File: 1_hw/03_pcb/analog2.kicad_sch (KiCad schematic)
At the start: 19 parts, among them U22 TPL0401B-10, U23 THS3491, U24 ADG1219BRJZ

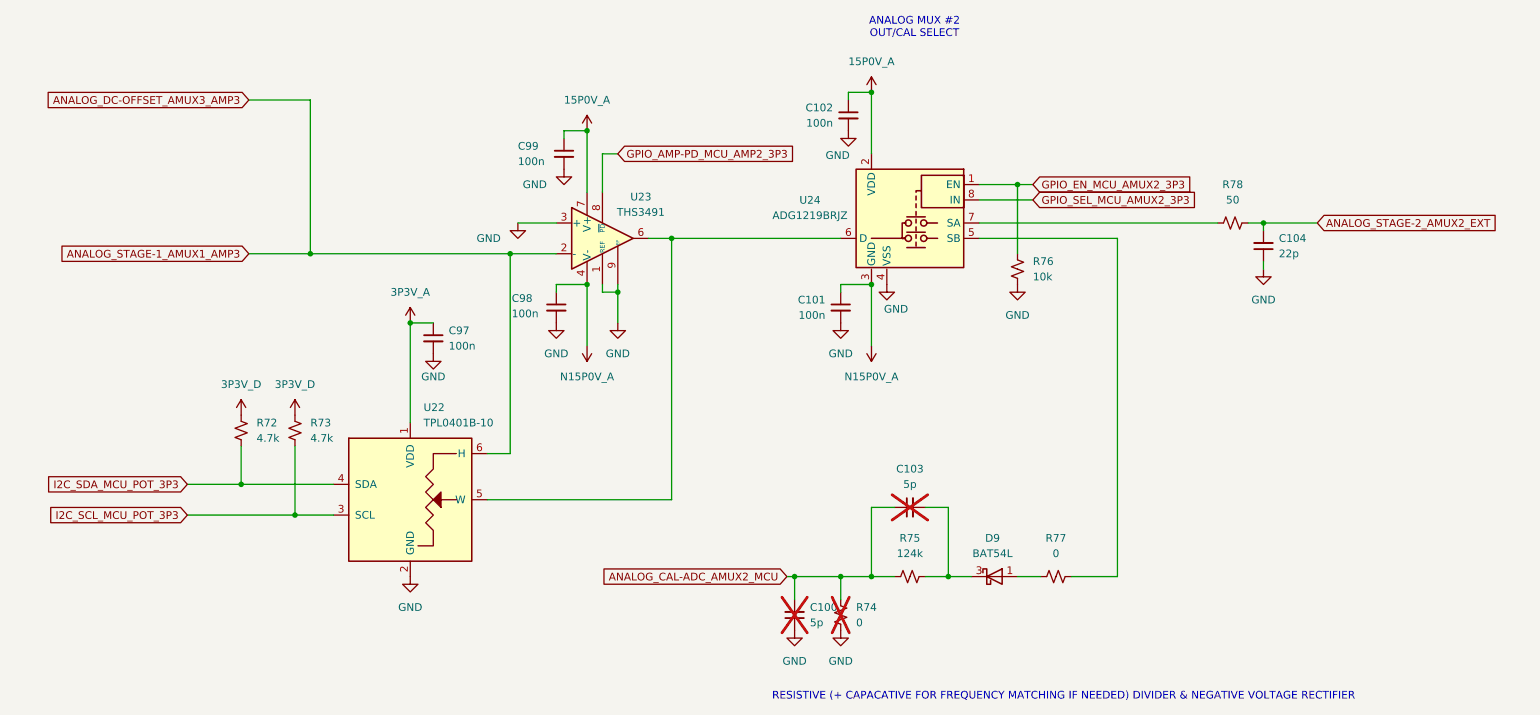
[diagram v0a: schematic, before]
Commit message: MINOR: Verified Footprints to Datasheets. Added Pull Ups on FPGA DONE/Config/SPI Chip Select Pins.
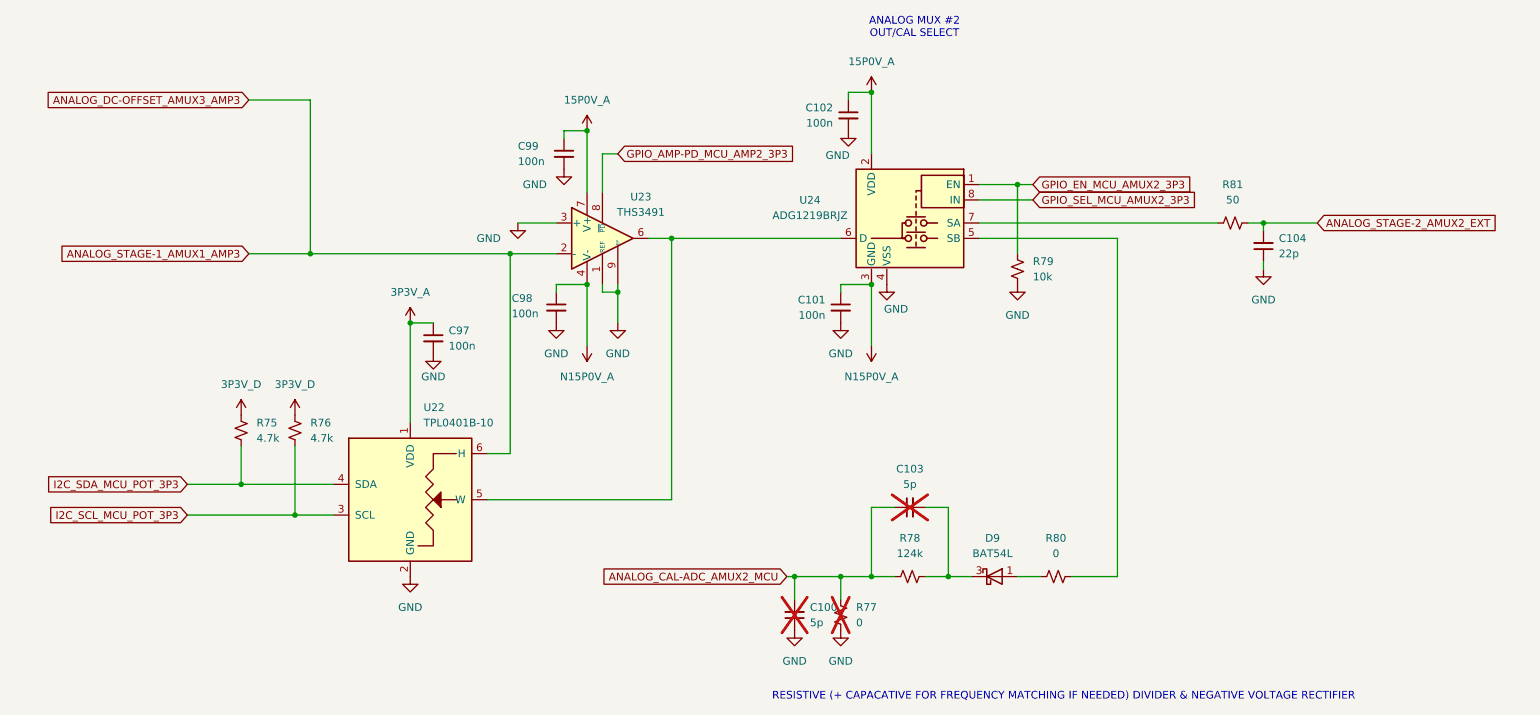
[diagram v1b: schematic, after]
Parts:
- renumbered R72 to R75, R73 to R76, R74 to R77, R75 to R78, R76 to R79, R77 to R80, R78 to R81
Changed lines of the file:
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@@
 		(dnp no)
 		(fields_autoplaced yes)
-		(property "Reference" "#PWR0257"
+		(property "Reference" "#PWR0260"
 			(at 152.4 104.14 0)
 			(effects
@@
 			(project "arb"
 				(path "/866ef9be-3b01-4288-a6e0-a2357aa17e50/e46c6640-71a3-4b78-b602-0f6be9676e36"
-					(reference "#PWR0257")
+					(reference "#PWR0260")
 					(unit 1)
 				)
@@
 		(dnp yes)
 		(fields_autoplaced yes)
-		(property "Reference" "R74"
+		(property "Reference" "R77"
 			(at 154.94 144.7799 0)
 			(effects
@@
 			(project "arb"
 				(path "/866ef9be-3b01-4288-a6e0-a2357aa17e50/e46c6640-71a3-4b78-b602-0f6be9676e36"
-					(reference "R74")
+					(reference "R77")
 					(unit 1)
 				)
@@
 		(dnp no)
 		(fields_autoplaced yes)
-		(property "Reference" "#PWR0258"
+		(property "Reference" "#PWR0261"
 			(at 152.4 154.94 0)
 			(effects
@@
 			(project "arb"
 				(path "/866ef9be-3b01-4288-a6e0-a2357aa17e50/e46c6640-71a3-4b78-b602-0f6be9676e36"
-					(reference "#PWR0258")
+					(reference "#PWR0261")
 					(unit 1)
 				)
@@
 		(dnp no)
 		(fields_autoplaced yes)
-		(property "Reference" "#PWR0254"
+		(property "Reference" "#PWR0257"
 			(at 110.49 97.79 0)
 			(effects
@@
 			(project "arb"
 				(path "/866ef9be-3b01-4288-a6e0-a2357aa17e50/e46c6640-71a3-4b78-b602-0f6be9676e36"
-					(reference "#PWR0254")
+					(reference "#PWR0257")
 					(unit 1)
 				)
@@
 		(dnp no)
 		(fields_autoplaced yes)
-		(property "Reference" "R76"
+		(property "Reference" "R79"
 			(at 184.15 87.6299 0)
 			(effects
@@
 			(project "arb"
 				(path "/866ef9be-3b01-4288-a6e0-a2357aa17e50/e46c6640-71a3-4b78-b602-0f6be9676e36"
-					(reference "R76")
+					(reference "R79")
 					(unit 1)
 				)
@@
 		(dnp no)
 		(fields_autoplaced yes)
-		(property "Reference" "#PWR0256"
+		(property "Reference" "#PWR0259"
 			(at 144.78 154.94 0)
 			(effects
@@
 			(project "arb"
 				(path "/866ef9be-3b01-4288-a6e0-a2357aa17e50/e46c6640-71a3-4b78-b602-0f6be9676e36"
-					(reference "#PWR0256")
+					(reference "#PWR0259")
 					(unit 1)
 				)
@@
 		(on_board yes)
 		(dnp no)
-		(property "Reference" "#PWR0259"
+		(property "Reference" "#PWR0262"
 			(at 153.67 72.39 0)
 			(effects
@@
 			(project "arb"
 				(path "/866ef9be-3b01-4288-a6e0-a2357aa17e50/e46c6640-71a3-4b78-b602-0f6be9676e36"
-					(reference "#PWR0259")
+					(reference "#PWR0262")
 					(unit 1)
 				)
@@
 		(dnp no)
 		(fields_autoplaced yes)
-		(property "Reference" "#PWR0255"
+		(property "Reference" "#PWR0258"
 			(at 115.57 104.14 0)
 			(effects
@@
 			(project "arb"
 				(path "/866ef9be-3b01-4288-a6e0-a2357aa17e50/e46c6640-71a3-4b78-b602-0f6be9676e36"
-					(reference "#PWR0255")
+					(reference "#PWR0258")
 					(unit 1)
 				)
@@
 		(dnp no)
 		(fields_autoplaced yes)
-		(property "Reference" "R75"
+		(property "Reference" "R78"
 			(at 163.83 133.35 90)
 			(effects
@@
 			(project "arb"
 				(path "/866ef9be-3b01-4288-a6e0-a2357aa17e50/e46c6640-71a3-4b78-b602-0f6be9676e36"
-					(reference "R75")
+					(reference "R78")
 					(unit 1)
 				)
@@
 		(on_board yes)
 		(dnp no)
-		(property "Reference" "#PWR0252"
+		(property "Reference" "#PWR0255"
 			(at 106.68 78.74 0)
 			(effects
@@
 			(project "arb"
 				(path "/866ef9be-3b01-4288-a6e0-a2357aa17e50/e46c6640-71a3-4b78-b602-0f6be9676e36"
-					(reference "#PWR0252")
+					(reference "#PWR0255")
 					(unit 1)
 				)
@@
 		(dnp no)
 		(fields_autoplaced yes)
-		(property "Reference" "#PWR0247"
+		(property "Reference" "#PWR0250"
 			(at 81.28 101.6 0)
 			(effects
@@
 			(project "arb"
 				(path "/866ef9be-3b01-4288-a6e0-a2357aa17e50/e46c6640-71a3-4b78-b602-0f6be9676e36"
-					(reference "#PWR0247")
+					(reference "#PWR0250")
 					(unit 1)
 				)
@@
 		(dnp no)
 		(fields_autoplaced yes)
-		(property "Reference" "R77"
+		(property "Reference" "R80"
 			(at 187.96 133.35 90)
 			(effects
@@
 			(project "arb"
 				(path "/866ef9be-3b01-4288-a6e0-a2357aa17e50/e46c6640-71a3-4b78-b602-0f6be9676e36"
-					(reference "R77")
+					(reference "R80")
 					(unit 1)
 				)
@@
 		(dnp no)
 		(fields_autoplaced yes)
-		(property "Reference" "#PWR0263"
+		(property "Reference" "#PWR0266"
 			(at 181.61 97.79 0)
 			(effects
@@
 			(project "arb"
 				(path "/866ef9be-3b01-4288-a6e0-a2357aa17e50/e46c6640-71a3-4b78-b602-0f6be9676e36"
-					(reference "#PWR0263")
+					(reference "#PWR0266")
 					(unit 1)
 				)
@@
 		(dnp no)
 		(fields_autoplaced yes)
-		(property "Reference" "#PWR0261"
+		(property "Reference" "#PWR0264"
 			(at 157.48 97.79 0)
 			(effects
@@
 			(project "arb"
 				(path "/866ef9be-3b01-4288-a6e0-a2357aa17e50/e46c6640-71a3-4b78-b602-0f6be9676e36"
-					(reference "#PWR0261")
+					(reference "#PWR0264")
 					(unit 1)
 				)
@@
 		(dnp no)
 		(fields_autoplaced yes)
-		(property "Reference" "R73"
+		(property "Reference" "R76"
 			(at 64.77 114.2999 0)
 			(effects
@@
 			(project "arb"
 				(path "/866ef9be-3b01-4288-a6e0-a2357aa17e50/e46c6640-71a3-4b78-b602-0f6be9676e36"
-					(reference "R73")
+					(reference "R76")
 					(unit 1)
 				)
@@
 		(dnp no)
 		(fields_autoplaced yes)
-		(property "Reference" "#PWR0245"
+		(property "Reference" "#PWR0248"
 			(at 53.34 116.84 0)
 			(effects
@@
 			(project "arb"
 				(path "/866ef9be-3b01-4288-a6e0-a2357aa17e50/e46c6640-71a3-4b78-b602-0f6be9676e36"
-					(reference "#PWR0245")
+					(reference "#PWR0248")
 					(unit 1)
 				)
@@
 		(dnp no)
 		(fields_autoplaced yes)
-		(property "Reference" "R78"
+		(property "Reference" "R81"
 			(at 217.17 74.93 90)
 			(effects
@@
 			(project "arb"
 				(path "/866ef9be-3b01-4288-a6e0-a2357aa17e50/e46c6640-71a3-4b78-b602-0f6be9676e36"
-					(reference "R78")
+					(reference "R81")
 					(unit 1)
 				)
@@
 		(on_board yes)
 		(dnp no)
-		(property "Reference" "#PWR0262"
+		(property "Reference" "#PWR0265"
 			(at 160.02 97.79 0)
 			(effects
@@
 			(project "arb"
 				(path "/866ef9be-3b01-4288-a6e0-a2357aa17e50/e46c6640-71a3-4b78-b602-0f6be9676e36"
-					(reference "#PWR0262")
+					(reference "#PWR0265")
 					(unit 1)
 				)
@@
 		(dnp no)
 		(fields_autoplaced yes)
-		(property "Reference" "#PWR0251"
+		(property "Reference" "#PWR0254"
 			(at 105.41 104.14 0)
 			(effects
@@
 			(project "arb"
 				(path "/866ef9be-3b01-4288-a6e0-a2357aa17e50/e46c6640-71a3-4b78-b602-0f6be9676e36"
-					(reference "#PWR0251")
+					(reference "#PWR0254")
 					(unit 1)
 				)
@@
 		(dnp no)
 		(fields_autoplaced yes)
-		(property "Reference" "#PWR0246"
+		(property "Reference" "#PWR0249"
 			(at 62.23 116.84 0)
 			(effects
@@
 			(project "arb"
 				(path "/866ef9be-3b01-4288-a6e0-a2357aa17e50/e46c6640-71a3-4b78-b602-0f6be9676e36"
-					(reference "#PWR0246")
+					(reference "#PWR0249")
 					(unit 1)
 				)
@@
 		(dnp no)
 		(fields_autoplaced yes)
-		(property "Reference" "#PWR0248"
+		(property "Reference" "#PWR0251"
 			(at 81.28 146.05 0)
 			(effects
@@
 			(project "arb"
 				(path "/866ef9be-3b01-4288-a6e0-a2357aa17e50/e46c6640-71a3-4b78-b602-0f6be9676e36"
-					(reference "#PWR0248")
+					(reference "#PWR0251")
 					(unit 1)
 				)
@@
 		(dnp no)
 		(fields_autoplaced yes)
-		(property "Reference" "R72"
+		(property "Reference" "R75"
 			(at 55.88 114.2999 0)
 			(effects
@@
 			(project "arb"
 				(path "/866ef9be-3b01-4288-a6e0-a2357aa17e50/e46c6640-71a3-4b78-b602-0f6be9676e36"
-					(reference "R72")
+					(reference "R75")
 					(unit 1)
 				)
@@
 		(on_board yes)
 		(dnp no)
-		(property "Reference" "#PWR0249"
+		(property "Reference" "#PWR0252"
 			(at 85.09 109.22 0)
 			(effects
@@
 			(project "arb"
 				(path "/866ef9be-3b01-4288-a6e0-a2357aa17e50/e46c6640-71a3-4b78-b602-0f6be9676e36"
-					(reference "#PWR0249")
+					(reference "#PWR0252")
 					(unit 1)
 				)
@@
 		(dnp no)
 		(fields_autoplaced yes)
-		(property "Reference" "#PWR0260"
+		(property "Reference" "#PWR0263"
 			(at 157.48 63.5 0)
 			(effects
@@
 			(project "arb"
 				(path "/866ef9be-3b01-4288-a6e0-a2357aa17e50/e46c6640-71a3-4b78-b602-0f6be9676e36"
-					(reference "#PWR0260")
+					(reference "#PWR0263")
 					(unit 1)
 				)
@@
 		(dnp no)
 		(fields_autoplaced yes)
-		(property "Reference" "#PWR0253"
+		(property "Reference" "#PWR0256"
 			(at 110.49 69.85 0)
 			(effects
@@
 			(project "arb"
 				(path "/866ef9be-3b01-4288-a6e0-a2357aa17e50/e46c6640-71a3-4b78-b602-0f6be9676e36"
-					(reference "#PWR0253")
+					(reference "#PWR0256")
 					(unit 1)
 				)
@@
 		(dnp no)
 		(fields_autoplaced yes)
-		(property "Reference" "#PWR0264"
+		(property "Reference" "#PWR0267"
 			(at 222.25 95.25 0)
 			(effects
@@
 			(project "arb"
 				(path "/866ef9be-3b01-4288-a6e0-a2357aa17e50/e46c6640-71a3-4b78-b602-0f6be9676e36"
-					(reference "#PWR0264")
+					(reference "#PWR0267")
 					(unit 1)
 				)
@@
 		(on_board yes)
 		(dnp no)
-		(property "Reference" "#PWR0250"
+		(property "Reference" "#PWR0253"
 			(at 99.06 87.63 0)
 			(effects
@@
 			(project "arb"
 				(path "/866ef9be-3b01-4288-a6e0-a2357aa17e50/e46c6640-71a3-4b78-b602-0f6be9676e36"
-					(reference "#PWR0250")
-					(unit 1)
-				)
+					(reference "#PWR0253")
+					(unit 1)
+				)
